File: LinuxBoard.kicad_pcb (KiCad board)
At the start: 4 copper layers, 186 parts, among them J1 Wuerth_7499010121A, J2 Conn_02x10_Counter_Clockwise, J3 Micro_SD_Card, J4 USB_A, J5 Conn_ARM_JTAG_SWD_10, J6 USB_B_Micro, J7 Barrel_Jack_Switch, SW1 SW_DIP_x03, SW2 SW_Push, SW3 SW_Push, SW4 SW_Push, SW5 SW_Push, U1 STM32MP151AAB3, U2 MT41K64M16TW-107_AAT_J_TR, U3 DP83848C, U4 STPMIC1APQR, Y1 24MHz, Y2 32.768KHz, Y3 25MHz

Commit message: Schematic signoff
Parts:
- removed the R29 at (121.7, 127.6)
- removed the R30 at (121.9, 125.0)
- removed R31: 10K, Resistor_SMD:R_0603_1608Metric_Pad1.05x0.95mm_HandSolder
- R30: value 10K -> 100
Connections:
- J5 pad 7: Net-(J5-Pad7) -> (no net)
- J5 pad 8: Net-(J5-Pad8) -> (no net)
- J6 pad 4: Net-(J6-Pad4) -> (no net)
- R29 pad 1: Net-(J5-Pad17) -> /RAM/CKE
- R30 pad 1: Net-(J5-Pad19) -> /RAM/CK_N
- R30 pad 2: GND -> /RAM/CK_P
- U1 pad A12: Net-(U1-PadA12) -> (no net)
- U1 pad A13: Net-(U1-PadA13) -> (no net)
- U1 pad A14: Net-(U1-PadA14) -> (no net)
- U1 pad A15: Net-(U1-PadA15) -> (no net)
- U1 pad A16: Net-(U1-PadA16) -> (no net)
- U1 pad A3: Net-(U1-PadA3) -> (no net)
- U1 pad A4: Net-(U1-PadA4) -> (no net)
- U1 pad A5: Net-(U1-PadA5) -> (no net)
- U1 pad A6: Net-(U1-PadA6) -> (no net)
- U1 pad A7: /MPU/SPI1_SCK -> (no net)
- U1 pad A9: Net-(U1-PadA9) -> (no net)
- U1 pad B1: Net-(U1-PadB1) -> (no net)
- U1 pad B11: Net-(U1-PadB11) -> (no net)
- U1 pad B12: Net-(U1-PadB12) -> (no net)
- U1 pad B13: Net-(U1-PadB13) -> (no net)
- U1 pad B14: Net-(U1-PadB14) -> (no net)
- U1 pad B15: Net-(U1-PadB15) -> (no net)
- U1 pad B16: Net-(U1-PadB16) -> (no net)
- U1 pad B7: Net-(U1-PadB7) -> (no net)
- U1 pad B8: Net-(U1-PadB8) -> (no net)
- U1 pad B9: /MPU/SPI1_MISO -> (no net)
- U1 pad C1: Net-(U1-PadC1) -> (no net)
- U1 pad C2: Net-(U1-PadC2) -> (no net)
- U1 pad C4: Net-(U1-PadC4) -> (no net)
- U1 pad C7: Net-(U1-PadC7) -> (no net)
- U1 pad C9: Net-(U1-PadC9) -> (no net)
- U1 pad D10: Net-(U1-PadD10) -> (no net)
- U1 pad D11: Net-(U1-PadD11) -> (no net)
- U1 pad D12: Net-(U1-PadD12) -> (no net)
- U1 pad D13: Net-(U1-PadD13) -> (no net)
- U1 pad D3: Net-(U1-PadD3) -> (no net)
- U1 pad D9: Net-(U1-PadD9) -> (no net)
- U1 pad E1: Net-(U1-PadE1) -> (no net)
- U1 pad F17: Net-(U1-PadF17) -> (no net)
- U1 pad J19: Net-(U1-PadJ19) -> (no net)
- U1 pad K18: Net-(U1-PadK18) -> (no net)
- U1 pad L16: Net-(U1-PadL16) -> (no net)
- U1 pad N18: Net-(U1-PadN18) -> (no net)
- U1 pad N19: Net-(U1-PadN19) -> (no net)
- U1 pad P1: Net-(U1-PadP1) -> (no net)
- U1 pad P2: Net-(U1-PadP2) -> (no net)
- U1 pad R1: Net-(U1-PadR1) -> (no net)
- U1 pad T10: Net-(U1-PadT10) -> (no net)
- U1 pad T11: Net-(U1-PadT11) -> (no net)
- U1 pad T13: Net-(U1-PadT13) -> (no net)
- U1 pad T14: Net-(U1-PadT14) -> (no net)
- U1 pad T16: Net-(U1-PadT16) -> (no net)
- U1 pad T5: Net-(U1-PadT5) -> (no net)
- U1 pad T7: Net-(U1-PadT7) -> (no net)
- U1 pad T8: /MPU/SPI1_MOSI -> (no net)
- U1 pad U1: Net-(U1-PadU1) -> (no net)
- U1 pad U10: Net-(U1-PadU10) -> (no net)
- U1 pad U16: Net-(U1-PadU16) -> (no net)
- U1 pad U7: Net-(U1-PadU7) -> (no net)
- U1 pad U9: Net-(U1-PadU9) -> (no net)
- U1 pad V10: Net-(U1-PadV10) -> (no net)
- U1 pad V17: Net-(U1-PadV17) -> (no net)
- U1 pad V5: Net-(U1-PadV5) -> (no net)
- U1 pad V7: Net-(U1-PadV7) -> (no net)
- U1 pad W10: Net-(U1-PadW10) -> (no net)
- U1 pad W6: Net-(U1-PadW6) -> (no net)
- U1 pad W7: Net-(U1-PadW7) -> (no net)
- U1 pad W9: Net-(U1-PadW9) -> (no net)
- U2 pad J1: Net-(U2-PadJ1) -> (no net)
- U2 pad J9: Net-(U2-PadJ9) -> (no net)
- U2 pad L1: Net-(U2-PadL1) -> (no net)
- U2 pad L9: Net-(U2-PadL9) -> (no net)
- U2 pad M7: Net-(U2-PadM7) -> (no net)
- U2 pad T3: Net-(U2-PadT3) -> (no net)
- U2 pad T7: Net-(U2-PadT7) -> (no net)
- U3 pad 27: Net-(U3-Pad27) -> (no net)

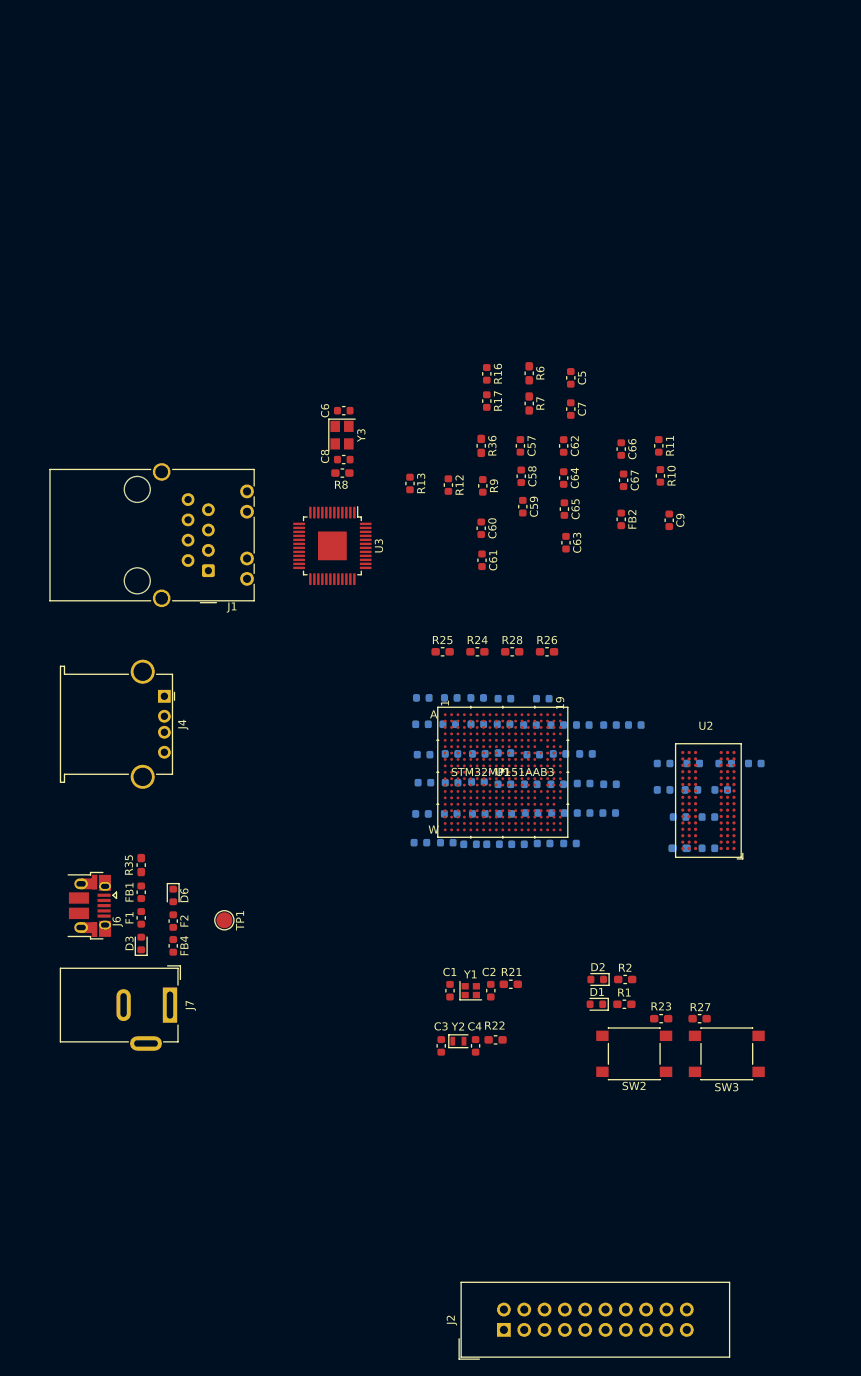
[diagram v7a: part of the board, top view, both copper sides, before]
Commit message: Fan out BGA
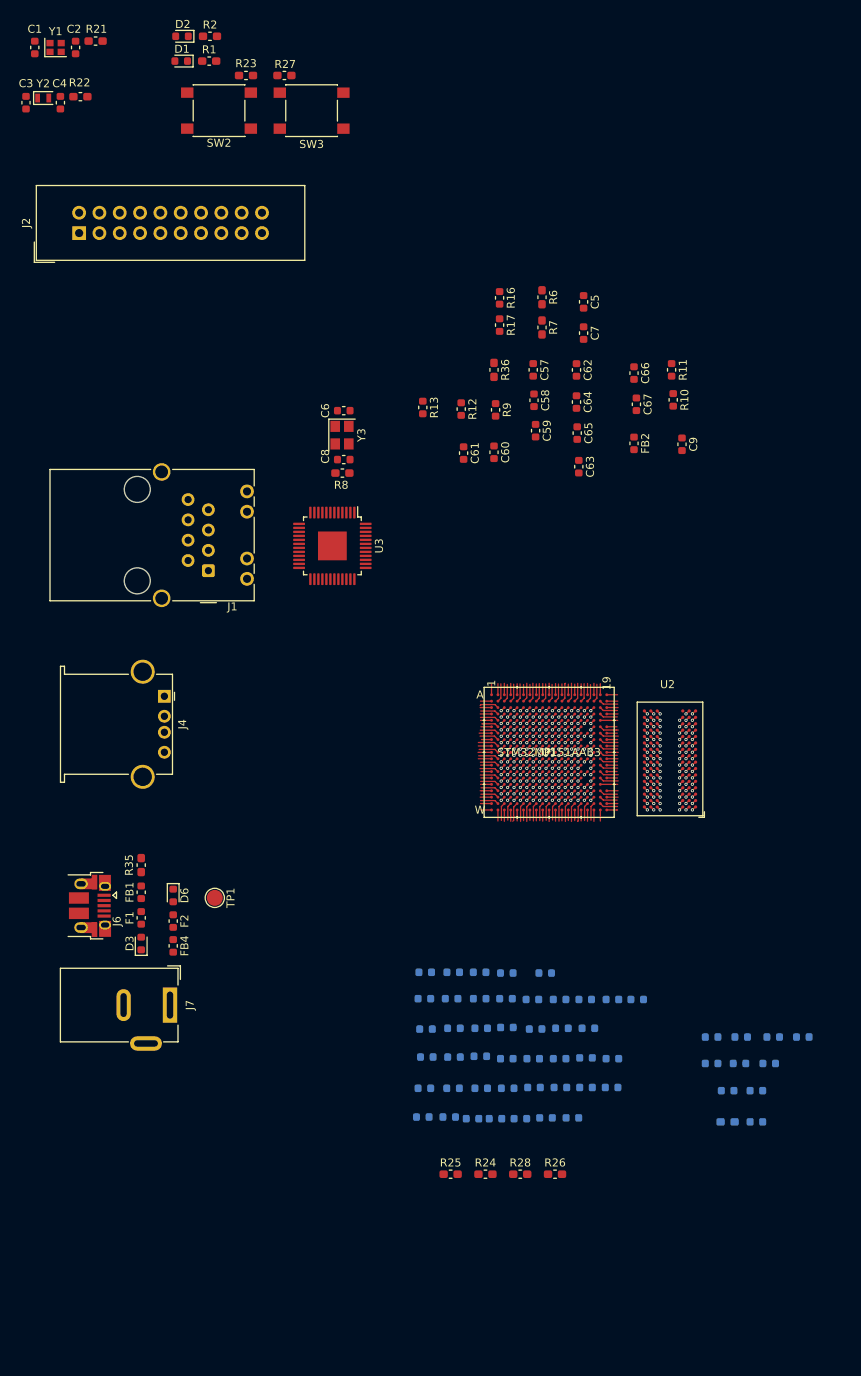
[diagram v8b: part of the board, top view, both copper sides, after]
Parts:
- moved J2 147.0 mm to (36.8, 54.6)
- moved C1 128.8 mm to (31.3, 31.4)
- moved C2 128.8 mm to (36.4, 31.4)
- moved C3 128.8 mm to (30.2, 38.3)
- moved C4 128.8 mm to (34.5, 38.3)
- moved D1 128.8 mm to (49.6, 33.1)
- moved D2 128.8 mm to (49.7, 30.0)
- moved R1 128.8 mm to (53.1, 33.1)
- moved R2 128.8 mm to (53.2, 30.0)
- moved R21 128.8 mm to (38.9, 30.6)
- moved R22 128.8 mm to (37.0, 37.5)
- moved R23 128.8 mm to (57.7, 34.9)
- moved R27 128.8 mm to (62.5, 34.9)
- moved SW2 128.8 mm to (54.3, 39.3)
- moved SW3 128.8 mm to (65.9, 39.3)
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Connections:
- J5 pad 7: (no net) -> Net-(J5-Pad7)
- J5 pad 8: (no net) -> Net-(J5-Pad8)
- J6 pad 4: (no net) -> Net-(J6-Pad4)
- U1 pad A12: (no net) -> Net-(U1-PadA12)
- U1 pad A13: (no net) -> Net-(U1-PadA13)
- U1 pad A14: (no net) -> Net-(U1-PadA14)
- U1 pad A15: (no net) -> Net-(U1-PadA15)
- U1 pad A16: (no net) -> Net-(U1-PadA16)
- U1 pad A3: (no net) -> Net-(U1-PadA3)
- U1 pad A4: (no net) -> Net-(U1-PadA4)
- U1 pad A5: (no net) -> Net-(U1-PadA5)
- U1 pad A6: (no net) -> Net-(U1-PadA6)
- U1 pad A7: (no net) -> /MPU/SPI1_SCK
- U1 pad A9: (no net) -> Net-(U1-PadA9)
- U1 pad B1: (no net) -> Net-(U1-PadB1)
- U1 pad B11: (no net) -> Net-(U1-PadB11)
- U1 pad B12: (no net) -> Net-(U1-PadB12)
- U1 pad B13: (no net) -> Net-(U1-PadB13)
- U1 pad B14: (no net) -> Net-(U1-PadB14)
- U1 pad B15: (no net) -> Net-(U1-PadB15)
- U1 pad B16: (no net) -> Net-(U1-PadB16)
- U1 pad B7: (no net) -> Net-(U1-PadB7)
- U1 pad B8: (no net) -> Net-(U1-PadB8)
- U1 pad B9: (no net) -> /MPU/SPI1_MISO
- U1 pad C1: (no net) -> Net-(U1-PadC1)
- U1 pad C2: (no net) -> Net-(U1-PadC2)
- U1 pad C4: (no net) -> Net-(U1-PadC4)
- U1 pad C7: (no net) -> Net-(U1-PadC7)
- U1 pad C9: (no net) -> Net-(U1-PadC9)
- U1 pad D10: (no net) -> Net-(U1-PadD10)
- U1 pad D11: (no net) -> Net-(U1-PadD11)
- U1 pad D12: (no net) -> Net-(U1-PadD12)
- U1 pad D13: (no net) -> Net-(U1-PadD13)
- U1 pad D3: (no net) -> Net-(U1-PadD3)
- U1 pad D9: (no net) -> Net-(U1-PadD9)
- U1 pad E1: (no net) -> Net-(U1-PadE1)
- U1 pad F17: (no net) -> Net-(U1-PadF17)
- U1 pad J19: (no net) -> Net-(U1-PadJ19)
- U1 pad K18: (no net) -> Net-(U1-PadK18)
- U1 pad L16: (no net) -> Net-(U1-PadL16)
- U1 pad N18: (no net) -> Net-(U1-PadN18)
- U1 pad N19: (no net) -> Net-(U1-PadN19)
- U1 pad P1: (no net) -> Net-(U1-PadP1)
- U1 pad P2: (no net) -> Net-(U1-PadP2)
- U1 pad R1: (no net) -> Net-(U1-PadR1)
- U1 pad T10: (no net) -> Net-(U1-PadT10)
- U1 pad T11: (no net) -> Net-(U1-PadT11)
- U1 pad T13: (no net) -> Net-(U1-PadT13)
- U1 pad T14: (no net) -> Net-(U1-PadT14)
- U1 pad T16: (no net) -> Net-(U1-PadT16)
- U1 pad T5: (no net) -> Net-(U1-PadT5)
- U1 pad T7: (no net) -> Net-(U1-PadT7)
- U1 pad T8: (no net) -> /MPU/SPI1_MOSI
- U1 pad U1: (no net) -> Net-(U1-PadU1)
- U1 pad U10: (no net) -> Net-(U1-PadU10)
- U1 pad U16: (no net) -> Net-(U1-PadU16)
- U1 pad U7: (no net) -> Net-(U1-PadU7)
- U1 pad U9: (no net) -> Net-(U1-PadU9)
- U1 pad V10: (no net) -> Net-(U1-PadV10)
- U1 pad V17: (no net) -> Net-(U1-PadV17)
- U1 pad V5: (no net) -> Net-(U1-PadV5)
- U1 pad V7: (no net) -> Net-(U1-PadV7)
- U1 pad W10: (no net) -> Net-(U1-PadW10)
- U1 pad W6: (no net) -> Net-(U1-PadW6)
- U1 pad W7: (no net) -> Net-(U1-PadW7)
- U1 pad W9: (no net) -> Net-(U1-PadW9)
- U2 pad J1: (no net) -> Net-(U2-PadJ1)
- U2 pad J9: (no net) -> Net-(U2-PadJ9)
- U2 pad L1: (no net) -> Net-(U2-PadL1)
- U2 pad L9: (no net) -> Net-(U2-PadL9)
- U2 pad M7: (no net) -> Net-(U2-PadM7)
- U2 pad T3: (no net) -> Net-(U2-PadT3)
- U2 pad T7: (no net) -> Net-(U2-PadT7)
- U3 pad 27: (no net) -> Net-(U3-Pad27)
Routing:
- net GND: track 0.00 -> 86.0 mm, vias 0 -> 109
- net /MPU_Power/PMIC_VDD_CORE: track 0.00 -> 18.9 mm, vias 0 -> 34
- net /MPU_Power/VDDQ_DDR: track 0.00 -> 15.5 mm, vias 0 -> 29
- net /VDD: track 0.00 -> 14.3 mm, vias 0 -> 19
- net /RAM/NRST: track 0.00 -> 4.28 mm
- net /RAM/A2: track 0.00 -> 2.91 mm, vias 0 -> 1
- net /RAM/DQ8: track 0.00 -> 2.90 mm, vias 0 -> 1
- net /RAM/A0: track 0.00 -> 2.87 mm, vias 0 -> 1
- net /RAM/DQ13: track 0.00 -> 2.87 mm, vias 0 -> 1
- net /RAM/A11: track 0.00 -> 2.85 mm, vias 0 -> 1
- net /RAM/DQ7: track 0.00 -> 2.85 mm, vias 0 -> 1
- net /RAM/CS_N: track 0.00 -> 2.84 mm, vias 0 -> 1
- net /RAM/DQ14: track 0.00 -> 2.82 mm, vias 0 -> 1
- net /RAM/RAS_N: track 0.00 -> 2.81 mm, vias 0 -> 1
- net /RAM/LDM: track 0.00 -> 2.81 mm, vias 0 -> 1
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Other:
- net class Default: clearance 0.2 -> 0.127; trace_width 0.25 -> 0.127; via_dia 0.8 -> 0.4; via_drill 0.4 -> 0.2
- net class JLC added: clearance 0.127, trace_width 0.127, via_dia 0.4, via_drill 0.2
- rule trace_clearance: 0.2 -> 0.127
- rule trace_min: 0.2 -> 0.127
- rule via_min_drill: 0.3 -> 0.2
